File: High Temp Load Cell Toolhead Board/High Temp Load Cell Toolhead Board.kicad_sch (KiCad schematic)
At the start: 118 parts, among them J1 Conn_01x03, J11 Conn_01x03, J12 Conn_01x03, J13 PinHeader_2x4_P2.54mm, J2 Conn_02x08, J6 Conn_01x04, J7 Conn_01x02, J8 Conn_01x04, J9 Conn_01x02, P1 USB_C_Plug_USB2.0, Q1 DMG3404L, Q2 DMG3404L, SW1 SW_SPST, U1 MAX31865xTP, U2 STM32F103CBU6TR, U3 SN74LVC2G17DSFR, U4 SN74AHC1G32QDBVRQ1, U5 ADS1220, X1 ECS-2520MVLC-080-BP-TR

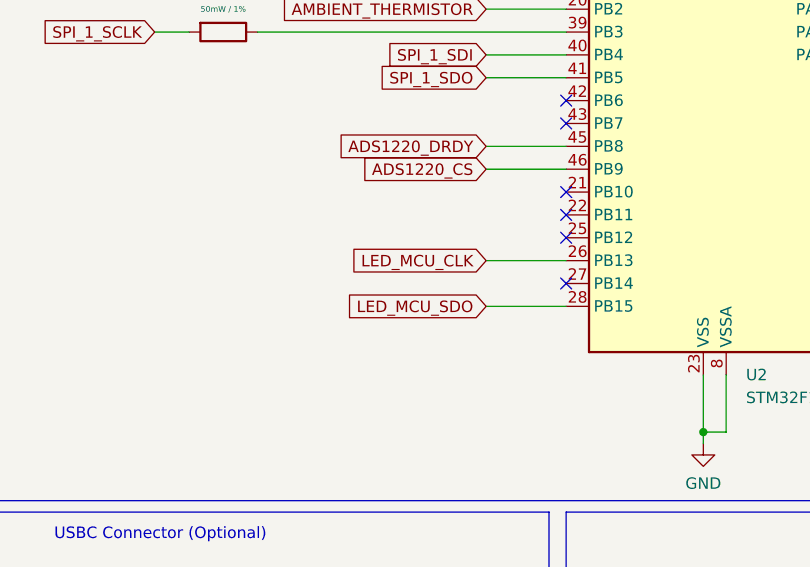
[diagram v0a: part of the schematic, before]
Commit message: USB Routing Improvement & Trach Width Change
* Fix net class assignment of USB lines so they autoroute with the correct rules.
* Moved the LED CLK line routing so it doesn't cross the USB lines
* Added a zone of ground fill on layer 3 to cover the USB traces on the back of the board
* Changes the standard track with to 15mil / 0.381mm. This is what OSH Park say is 50 Ohm in their process.

Fixup

Fixup
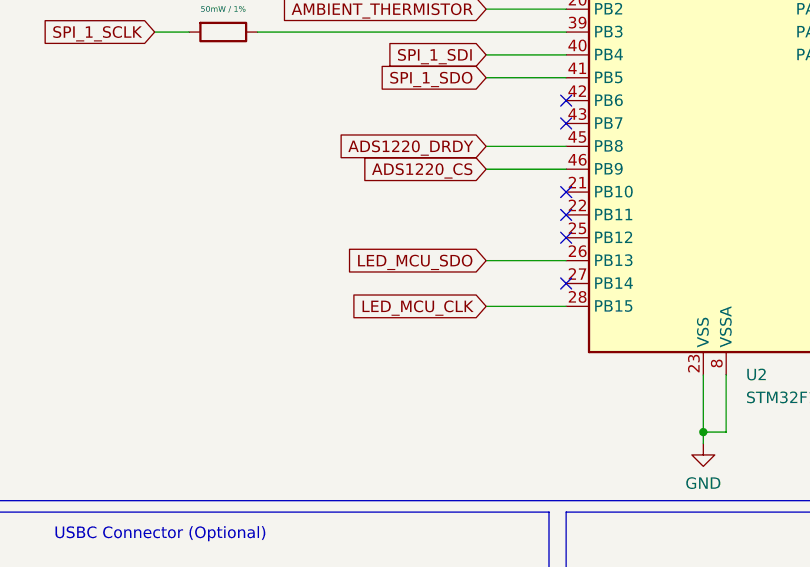
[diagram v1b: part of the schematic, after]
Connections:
- net LED_MCU_CLK: now also U2.28 (PB15); no longer U2.26 (PB13)
- net LED_MCU_SDO: now also U2.26 (PB13); no longer U2.28 (PB15)

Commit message: Replace Oscillator Module with Crystal
* After a bunch of research I've concluded that I cant use the Oscillator Module with Katapult's codebase for the STM32 chips. Added discussion on this to the design doc. Updated design to use a crystal and 2 caps. Exact capacitor values to be calculated later

* Based on the best advice I can find for decoupling capacitors on the MCU I have moved them to the back side of the board. This allows their footprints to overlap with the MCU itself, reducing the distance from the MCU to the decoupling cap. Also added vias next to the 2 pins  on the MCU that are true ground pins. There are other ground connections through GPIO pins but these are high impedance.

* Removed the power planes on layer 3 and replaced them with traces. With the additional components on the bottom layer, its more advantageous to have layer 3 be a ground reference for layer 4 in the places where items are routed on that layer. Power planes were easier to maintain but I don't think this board has any power delivery problems.

* Removed the extra diode and routing from the USB supply. Its not a requirement that the 5V rail power up from USB.
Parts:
- removed D16: 40V, 1A, SMA, Diode_SMD:D_SMA, symbol Device:D_Schottky
- removed X1: ECS-2520MVLC-080-BP-TR, Oscillator:Oscillator_SMD_ECS_2520MV-xxx-xx-4Pin_2.5x2.0mm, symbol Oscillator:ECS-2520MV-xxx-xx
- added C30, C33: 2?pF, Capacitor_SMD:C_0603_1608Metric, symbol Device:C
- added Y1: Crystal ECS-.327-6-34QCS-TR, ECS-.327-6-34QCS-TR:XTAL_ECS-.327-6-34QCS-TR, symbol Device:Crystal
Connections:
- net GND: now also U2.10 (PA0), U2.15 (PA5), U2.16 (PA6), U2.2 (PC13), U2.21 (PB10), U2.22 (PB11), U2.25 (PB12), U2.27 (PB14), U2.29 (PA8), U2.3 (PC14), U2.30 (PA9), U2.4 (PC15), U2.42 (PB6), U2.43 (PB7), C30.1, C33.1
- net OSC_IN: now reaches U2.5 (PD0)
- net OSC_IN: now also C30.2, Y1.2
- net OSC_OUT: now reaches U2.6 (PD1)
- net OSC_OUT: now also C33.2, Y1.1
- net SPI_1_SDO_OR_CS: now reaches AC1.13 (SDA/SDI/SDIO), U4.4
- net +5V_USB: now reaches D15.2 (A), P1.A4 (VBUS), P1.A9 (VBUS), P1.B4 (VBUS), P1.B9 (VBUS)
- no-connect marks 27 -> 11
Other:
- moved on the sheet: C20, C21, C22, C23, C24, C25, C26, D15, R13, R28, U2

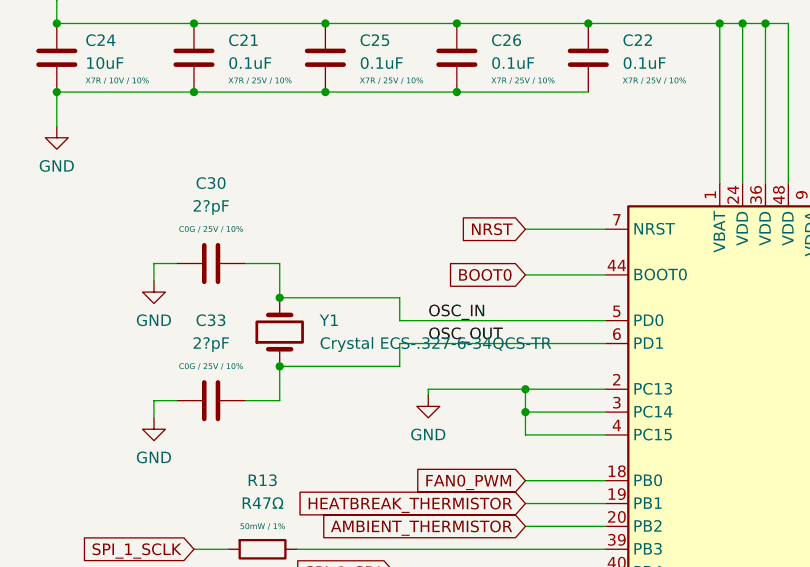
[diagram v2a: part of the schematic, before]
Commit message: Add Via Stitching
* Re-run via stitching on GND
* Add capacitor values to crystal caps
* Update design doc
* Remove bad assembly document
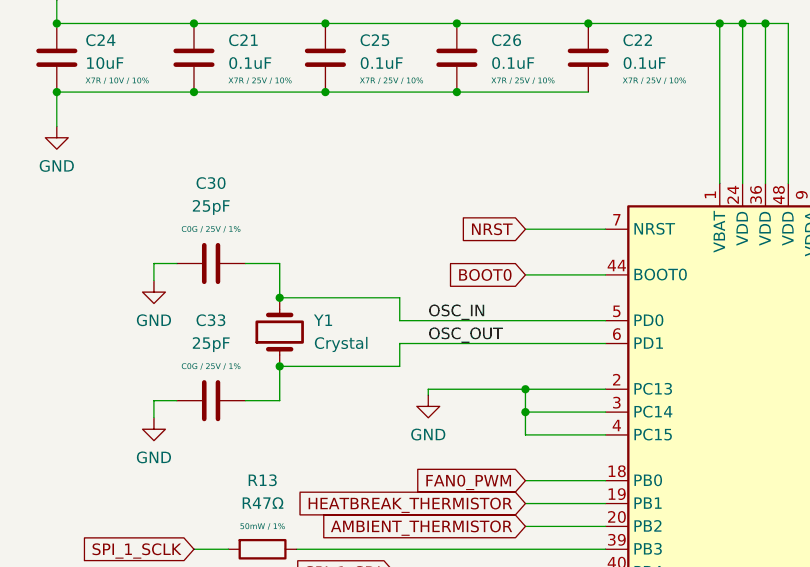
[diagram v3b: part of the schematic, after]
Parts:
- C30, C33: value 2?pF -> 25pF
- Y1: value Crystal ECS-.327-6-34QCS-TR -> Crystal
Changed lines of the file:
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@@
 			)
 		)
-		(property "Value" "2?pF"
+		(property "Value" "25pF"
 			(at 66.04 182.88 90)
 			(effects
@@
 			)
 		)
-		(property "Description" "C0G / 25V / 10%"
+		(property "Description" "C0G / 25V / 1%"
 			(at 66.04 185.42 90)
 			(effects
@@
 			)
 		)
-		(property "Value" "2?pF"
+		(property "Value" "25pF"
 			(at 66.04 198.12 90)
 			(effects
@@
 			)
 		)
-		(property "Description" "C0G / 25V / 10%"
+		(property "Description" "C0G / 25V / 1%"
 			(at 66.04 200.66 90)
 			(effects
@@
 		(fields_autoplaced yes)
 		(property "Reference" "Y1"
-			(at 78.105 195.5799 90)
+			(at 77.47 195.5799 90)
 			(effects
 				(font
@@
 			)
 		)
-		(property "Value" "Crystal ECS-.327-6-34QCS-TR"
-			(at 78.105 198.1199 90)
+		(property "Value" "Crystal"
+			(at 77.47 198.1199 90)
 			(effects
 				(font

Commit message: WIP Address community comments
* Switch to 6 layers and update design rules for new 6 layer process
* Change fan MOSFETs based on feedback. Drive MOSFETs with level shifter at 5V
* Add a 5V LDO for the loadcell thats not potentially poisoned by 5V LED noise
* Delete MAX chip, switch to PT1000
* Use 2 SPI busses, delete CS lines
* Move all components to front of board, re-organize layout to fit everything
* Switch to vertical USBC connector and import model

The schematic is updated but the routing has not been done
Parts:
- removed FID1, FID2, FID3: Fiducial, Fiducial:Fiducial_0.5mm_Mask1.5mm, symbol Mechanical:Fiducial
- removed R28: R430Ω, Resistor_SMD:R_0603_1608Metric, symbol Device:R
- removed U1: MAX31865xTP, Package_DFN_QFN:TQFN-20-1EP_5x5mm_P0.65mm_EP3.25x3.25mm, symbol Sensor_Temperature:MAX31865xTP
- removed U4: SN74AHC1G32QDBVRQ1, Package_TO_SOT_SMD:SOT-23-5, symbol 74xGxx:74AHC1G32
- added C37, C38: 0.1uF, Capacitor_SMD:C_0603_1608Metric, symbol Device:C
- added D16: RED LED, LED_SMD:LED_0603_1608Metric, symbol Device:LED
- added LDO3: TPS7A21-Q1 5V @ 500mA, Package_SON:VSON-8-1EP_3x3mm_P0.65mm_EP1.65x2.4mm_ThermalVias, symbol Project_Symbols:TPS7A21-Q1
- added R29: R1kΩ, Resistor_SMD:R_0603_1608Metric, symbol Device:R
- added R30, R32: R4.7kΩ, Resistor_SMD:R_0603_1608Metric, symbol Device:R
- added R31: R2.2kΩ, Resistor_SMD:R_0603_1608Metric, symbol Device:R
- added R33: R47Ω, Resistor_SMD:R_0603_1608Metric, symbol Device:R
- added TP1: Test +3V3, symbol Connector:TestPoint
- added TP2: Test +5V5, symbol Connector:TestPoint
- added TP3: Test +5V, symbol Connector:TestPoint
- added TP4: Test +5VA, symbol Connector:TestPoint
- added U1: SN74LVC2G17DSFR, Package_TO_SOT_SMD:SOT-363_SC-70-6, symbol SN74LVC2G17DSFR:SN74LVC2G17DSFR
- C10, C9: value 0.1uF -> 10uF; footprint Capacitor_SMD:C_0603_1608Metric -> Capacitor_SMD:C_1206_3216Metric
- LDO1: value TPS7121-Q1 5V @ 500mA -> TPS7A21-Q1 5V @ 500mA
- LDO2: value TPS7121-Q1 3.3V @ 500mA -> TPS7A21-Q1 3.3V @ 500mA
- P1: footprint Connector_USB:USB_C_Receptacle_GCT_USB4110 -> GCT_USB4145-03-0170-C:USB4145030170C; Manufacturer_Part_Number USB4110-GF-A -> USB4145-03-0170-C; Supplier_Link https://www.digikey.com/en/products/detail/gct/USB4110-GF-A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 -> https://www.digikey.com/en/products/detail/gct/USB4145-03-0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; Supplier_Part_Number 2073-USB4110-GF-A-1-ND -> 2073-USB4145-03-0170-CCT-ND
- Q1, Q2: value DMG3404L -> CSD17581Q3A; footprint Package_TO_SOT_SMD:SOT-23 -> Package_SON:VSON-8_3.3x3.3mm_P0.65mm_NexFET; symbol Transistor_FET:DMG3404L -> Transistor_FET:CSD17581Q3A; MANUFACTURER (none) -> Texas Instruments; MAXIMUM_PACKAGE_HEIGHT (none) -> 0.9mm; Manufacturer_Name Diodes Incorporated -> Texas Instruments; Manufacturer_Part_Number DMG3404L-7 -> CSD17581Q3A; PARTREV (none) -> October 2016; STANDARD (none) -> Manufacturer Recommendations; Supplier_Link https://www.digikey.com/en/products/detail/diodes-incorpora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 -> https://www.digikey.com/en/products/detail/texas-instrument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; Supplier_Part_Number DMG3404L-7DICT-ND -> 296-47754-1-ND
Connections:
- net ADS1220_CS is gone; now on net GND: U2.46 (PB9), U5.2 (~{CS})
- net ADXL345_CS is gone; now on net GND: AC1.7 (~{CS}), U2.11 (PA1)
- net +3V3: now also R30.2, R31.2, TP1.1; no longer C11.1, C9.1
- net +5V: now also TP3.1, U1.5 (VCC); no longer C13.2, C17.1, C29.1, L2.2, U5.12 (AVDD), U5.9 (REFP0)
- net +5V5: now also C9.1, LDO3.5 (EN), LDO3.8 (VIN), TP2.1
- net FAN0_MOSFET_GND: now also Q1.5 (D); no longer Q1.3 (D)
- net FAN0_PWM: now also U1.1 (1A); no longer R18.2, R19.2
- net FAN0_TACH: now also C37.1
- net FAN1_MOSFET_GND: now also Q2.5 (D); no longer Q2.3 (D)
- net FAN1_PWM: now also U1.3 (2A); no longer R26.2, R8.2
- net FAN1_TACH: now also C11.1
- net GND: now also C10.2, L13.2, Q1.1 (S), Q1.3 (S), Q2.1 (S), Q2.3 (S), C37.2, C38.2, D16.1 (K), LDO3.2 (GND), LDO3.3 (GND), LDO3.4 (GND), LDO3.6 (GND), LDO3.7 (GND), LDO3.9 (GND), U1.2 (GND); no longer U2.27 (PB14), U2.29 (PA8), U2.42 (PB6), U2.43 (PB7)
- net LED_GND: now also J8.1 (Pin_1); no longer J8.4 (Pin_4)
- net LED_MCU_CLK: now also U2.43 (PB7); no longer U2.28 (PB15)
- net LED_MCU_SDO: now also U2.42 (PB6); no longer U2.26 (PB13)
- net LED_POWER: now also J8.4 (Pin_4); no longer J8.1 (Pin_1)
- net SPI_1_SCLK: no longer AC1.14 (SCL/SCLK)
- net SPI_1_SDI: no longer AC1.12 (SDO/ALT_ADDRESS)
- net at R19.1: now also Q1.4 (G); no longer Q1.1 (G)
- net at L12.1: now also R30.1, R31.1, R32.2; no longer C10.1
- net at R26.1: now also Q2.4 (G); no longer Q2.1 (G)
- net MAX31865_CS renamed PT1000
- net PT1000: now also C38.1, R32.1
- net PT100+ renamed PT1000+
- net PT100- renamed PT1000-
- net SPI_1_SDO_OR_CS renamed SPI_2_SDO
- net SPI_2_SDO: now also U2.28 (PB15)
- new net: R33.1, U2.26 (PB13)
- new net: D16.2 (A), R29.1
- new net +5VA: C10.1, C13.2, C17.1, C29.1, L2.2, LDO3.1 (VOUT), TP4.1, U5.12 (AVDD), U5.9 (REFP0)
- new net FAN0_PWM_+5V: R18.2, R19.2, U1.6 (1Y)
- new net FAN1_PWM_+5V: R26.2, R8.2, U1.4 (2Y)
- new net INDICATOR_LED: R29.2, U2.29 (PA8)
- new net SPI_2_SCLK: AC1.14 (SCL/SCLK), R33.2
- new net SPI_2_SDI: AC1.12 (SDO/ALT_ADDRESS), U2.27 (PB14)
- no-connect marks 11 -> 10
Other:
- note added: "3.3V to 5V Fan PWM Level Shifter"
- note added: "5.5V to 3.3V LDO"
- note added: "5.5V to 5V LED Power LDO"
- note added: "5.5V to 5V Load Cell Power LDO"
- note added: "PT1000 Port"
- note added: "Test Points"
- note removed: "6V to 3.3V LDO"
- note removed: "6V to 5V LDO"
- note removed: "MAX31865 RTD Sensor"
- moved on the sheet: C1, C12, C13, C14, C15, C16, C17, C2, C20, C21, C22, C23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

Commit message: Feedback Updates Completed
* Disconnected unused GPIO pins from ground, use software pulldown instead.
* Re-rout for OSHPark's 6 layer stackup
* Shrink reference text to 0.8mmx0.8mm and 5 mil thickness
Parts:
- removed R31: R2.2kΩ, Resistor_SMD:R_0603_1608Metric, symbol Device:R
- removed R32: R4.7kΩ, Resistor_SMD:R_0603_1608Metric, symbol Device:R
- removed TP1: Test +3V3, symbol Connector:TestPoint
- removed TP2: Test +5V5, symbol Connector:TestPoint
- removed TP3: Test +5V, symbol Connector:TestPoint
- removed TP4: Test +5VA, symbol Connector:TestPoint
- added D17: RED LED, LED_SMD:LED_0603_1608Metric, symbol Device:LED
- added R12: R2kΩ, Resistor_SMD:R_0603_1608Metric, symbol Device:R
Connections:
- net PT1000 is gone; now on net HOTEND_THERMISTOR: C38.1, U2.12 (PA2)
- net +5VA: now also R12.2
- net FAN0_TACH: now also U2.14 (PA4); no longer U2.17 (PA7)
- net FAN1_PWM: now also U2.15 (PA5); no longer U2.14 (PA4)
- net GND: now also D17.1 (K); no longer U2.10 (PA0), U2.11 (PA1), U2.15 (PA5), U2.16 (PA6), U2.2 (PC13), U2.21 (PB10), U2.22 (PB11), U2.25 (PB12), U2.3 (PC14), U2.30 (PA9), U2.4 (PC15), U2.46 (PB9)
- net HOTEND_THERMISTOR: now reaches L12.1, R30.1
- net AIN0: now reaches C14.1, C15.2, R17.1, U5.11 (AIN0/REFP1)
- net AIN1: now reaches C14.2, C16.1, R16.1, U5.10 (AIN1)
- net PT1000+ renamed HOTEND_TH_GND
- net HOTEND_TH_GND: now also L13.1; no longer L12.2
- net PT1000- renamed HOTEND_TH_VREF
- net HOTEND_TH_VREF: now also L12.2; no longer L13.1
- new net: D17.2 (A), R12.1
- no-connect marks 10 -> 22
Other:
- note added: "Hotend Thermistor"
- note removed: "PT1000 Port"
- note removed: "Test Points"
- moved on the sheet: AC1, C11, C12, C13, C14, C15, C16, C17, C19, C27, C28, C29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

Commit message: Update 5V Power input
* Changed 5V USB power to rout in via the main 24V power input. This assumes the buck converter can operate in dropout mode and pass the 5V supply to the LDOs. This avoids potential issues with backfeeding the buck converter.
* Added a klipper pins file to give meaningful names to pins
* Added do-not-populate bypass resistors for fans to test tachometer behavior
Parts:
- added R20, R24: R20kΩ, Resistor_SMD:R_0603_1608Metric, symbol Device:R
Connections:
- net +24V: now also D15.1 (K)
- net +5V5: no longer D15.1 (K)
- net FAN0_MOSFET_GND: now also R20.2
- net FAN1_MOSFET_GND: now also R24.2
- net GND: now also R20.1, R24.1
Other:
- moved on the sheet: C11, C37, D7, D8, Q1, Q2, R14, R18, R19, R26, R4, R8

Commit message: Add Dotstar Indicator
This change replaces the indicator LED with a Dotstar RGB LED. This allows various conditions to be indicated at the toolhead via colors, brightness and blinking.

* Fixed missing guard ring on layers 4 and 5.
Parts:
- removed D16: RED LED, LED_SMD:LED_0603_1608Metric, symbol Device:LED
- removed R29: R1kΩ, Resistor_SMD:R_0603_1608Metric, symbol Device:R
- added D16: DotStar Micro LED, LED_SMD:LED-APA102-2020, symbol LED:APA102-2020
- added U4: SN74LVC2G17DSFR, Package_TO_SOT_SMD:SOT-363_SC-70-6, symbol SN74LVC2G17DSFR:SN74LVC2G17DSFR
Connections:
- net +5V: now also D16.1 (VDD), U4.5 (VCC)
- net GND: now also D16.6 (GND), U4.2 (GND)
- net INDICATOR_LED_SDO: now reaches U2.30 (PA9)
- net INDICATOR_LED_SDO: now also U4.3 (2A)
- net INDICATOR_LED renamed INDICATOR_LED_CLK
- net INDICATOR_LED_CLK: now also U4.1 (1A)
- new net RGB_INDICATOR_CLK: D16.5 (CKI), U4.4 (2Y)
- new net RGB_INDICATOR_SDO: D16.4 (SDI), U4.6 (1Y)
- no-connect marks 22 -> 23
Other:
- note added: "RGB INDICATOR LED"
- moved on the sheet: D13, D14, D17, D2, D3, D5, D6, H1, H2, H3, H4, R10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

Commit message: Move Filament Switch & Heatbreak Thermistor to ADC Inputs
* Move Filament switch line from PA15 to PA7
* Move Heatberak Thermistor from PB1 to PA6 (PB1 is Boot1)
* Re-routed Filament switch line on the back side of the PCB
* Edited pin assignments for thermistors to make routing cleaner
* Updated pins file to reflect changes
* Renamed Neopixel port to Dotstar.
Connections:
- net AMBIENT_THERMISTOR: now also U2.19 (PB1); no longer U2.20 (PB2)
- net FILAMENT_SW: now also U2.17 (PA7); no longer U2.38 (PA15)
- net HEATBREAK_THERMISTOR: now also U2.16 (PA6); no longer U2.19 (PB1)
- net INDICATOR_LED_CLK renamed RGB_LED_CLOCK
- net INDICATOR_LED_SDO renamed RGB_LED_DATA
- net LED_MCU_CLK renamed DOTSTAR_LED_CLOCK
- net LED_MCU_SDO renamed DOTSTAR_LED_DATA
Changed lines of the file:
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@@
 	)
 	(no_connect
+		(at 138.43 221.615)
+	)
+	(no_connect
+		(at 105.41 216.535)
+	)
+	(no_connect
 		(at 67.945 317.5)
 	)
@@
 	)
 	(no_connect
-		(at 138.43 201.295)
-	)
-	(no_connect
 		(at 105.41 239.395)
 	)
@@
 	)
 	(no_connect
-		(at 138.43 198.755)
-	)
-	(no_connect
 		(at 560.705 191.77)
 	)
@@
 	(wire
 		(pts
+			(xy 140.335 198.755) (xy 138.43 198.755)
+		)
+		(stroke
+			(width 0)
+			(type default)
+		)
+	)
+	(wire
+		(pts
 			(xy 103.505 224.155) (xy 105.41 224.155)
 		)
@@
 	(wire
 		(pts
-			(xy 105.41 216.535) (xy 103.505 216.535)
-		)
-		(stroke
-			(width 0)
-			(type default)
-		)
-	)
-	(wire
-		(pts
 			(xy 441.325 379.73) (xy 441.325 374.015)
 		)
@@
 	(wire
 		(pts
+			(xy 140.335 201.295) (xy 138.43 201.295)
+		)
+		(stroke
+			(width 0)
+			(type default)
+		)
+	)
+	(wire
+		(pts
 			(xy 76.2 353.06) (xy 95.25 353.06)
 		)
@@
 	(wire
 		(pts
-			(xy 140.335 221.615) (xy 138.43 221.615)
-		)
-		(stroke
-			(width 0)
-			(type default)
-		)
-	)
-	(wire
-		(pts
 			(xy 52.705 180.34) (xy 52.705 195.58)
 		)
@@
 				)
 				(justify right)
+				(hide yes)
 			)
 		)
@@
 				)
 				(justify left)
+				(hide yes)
 			)
 		)
@@
 				)
 				(justify right)
+				(hide yes)
 			)
 		)
@@
 				)
 				(justify left)
+				(hide yes)
 			)
 		)
@@
 		)
 	)
+	(global_label "HEATBREAK_THERMISTOR"
+		(shape input)
+		(at 140.335 198.755 0)
+		(fields_autoplaced yes)
+		(effects
+			(font
+				(size 1.27 1.27)
+			)
+			(justify left)
+		)
+		(property "Intersheetrefs" "${INTERSHEET_REFS}"
+			(at 166.422 198.755 0)
+			(effects
+				(font
+					(size 1.27 1.27)
+				)
+				(justify left)
+				(hide yes)
+			)
+		)
+	)
 	(global_label "USB_PULL_UP"
 		(shape input)
@@
 		)
 	)
-	(global_label "HEATBREAK_THERMISTOR"
+	(global_label "FAN1_TACH"
 		(shape input)
-		(at 103.505 213.995 180)
+		(at 433.705 361.315 180)
 		(fields_autoplaced yes)
 		(effects
@@
 		)
 		(property "Intersheetrefs" "${INTERSHEET_REFS}"
-			(at 77.418 213.995 0)
+			(at 420.3783 361.315 0)
 			(effects
 				(font
@@
 		)
 	)
-	(global_label "FAN1_TACH"
+	(global_label "FILAMENT_SW"
 		(shape input)
-		(at 433.705 361.315 180)
+		(at 140.335 201.295 0)
 		(fields_autoplaced yes)
 		(effects
@@
 				(size 1.27 1.27)
 			)
-			(justify right)
+			(justify left)
 		)
 		(property "Intersheetrefs" "${INTERSHEET_REFS}"
-			(at 420.3783 361.315 0)
+			(at 155.6573 201.295 0)
 			(effects
 				(font
 					(size 1.27 1.27)
 				)
-				(justify right)
+				(justify left)
 				(hide yes)
 			)
 		)
 	)
-	(global_label "LED_MCU_SDO"
+	(global_label "DOTSTAR_LED_DATA"
 		(shape input)
 		(at 103.505 226.695 180)
@@
 		)
 	)
-	(global_label "AMBIENT_THERMISTOR"
-		(shape input)
-		(at 103.505 216.535 180)
-		(fields_autoplaced yes)
-		(effects
-			(font
-				(size 1.27 1.27)
-			)
-			(justify right)
-		)
-		(property "Intersheetrefs" "${INTERSHEET_REFS}"
-			(at 80.1394 216.535 0)
-			(effects
-				(font
-					(size 1.27 1.27)
-				)
-				(justify right)
-				(hide yes)
-			)
-		)
-	)
 	(global_label "FAN0_PWM"
 		(shape input)
@@
 		)
 	)
-	(global_label "INDICATOR_LED_CLK"
+	(global_label "RGB_LED_CLOCK"
 		(shape input)
 		(at 140.335 203.835 0)
@@
 		)
 	)
-	(global_label "FILAMENT_SW"
-		(shape input)
-		(at 140.335 221.615 0)
-		(fields_autoplaced yes)
-		(effects
-			(font
-				(size 1.27 1.27)
-			)
-			(justify left)
-		)
-		(property "Intersheetrefs" "${INTERSHEET_REFS}"
-			(at 155.6573 221.615 0)
-			(effects
-				(font
-					(size 1.27 1.27)
-				)
-				(justify left)
-				(hide yes)
-			)
-		)
-	)
 	(global_label "SW_CLK"
 		(shape input)
@@
 		)
 	)
-	(global_label "LED_MCU_CLK"
+	(global_label "DOTSTAR_LED_CLOCK"
 		(shape input)
 		(at 103.505 229.235 180)
@@
 		)
 	)
-	(global_label "INDICATOR_LED_SDO"
+	(global_label "RGB_LED_DATA"
 		(shape input)
 		(at 140.335 206.375 0)
@@
 		)
 	)
+	(global_label "AMBIENT_THERMISTOR"
+		(shape input)
+		(at 103.505 213.995 180)
+		(fields_autoplaced yes)
+		(effects
+			(font
+				(size 1.27 1.27)
+			)
+			(justify right)
+		)
+		(property "Intersheetrefs" "${INTERSHEET_REFS}"
+			(at 80.1394 213.995 0)
+			(effects
+				(font
+					(size 1.27 1.27)
+				)
+				(justify right)
+				(hide yes)
+			)
+		)
+	)
 	(global_label "SW_CLK"
 		(shape input)
@@
 		)
 	)
-	(global_label "INDICATOR_LED_CLK"
+	(global_label "RGB_LED_CLOCK"
 		(shape input)
 		(at 480.06 191.135 180)
@@
 		)
 	)
-	(global_label "LED_MCU_SDO"
+	(global_label "DOTSTAR_LED_DATA"
 		(shape input)
 		(at 288.29 52.705 180)
@@
 		)
 	)
-	(global_label "INDICATOR_LED_SDO"
+	(global_label "RGB_LED_DATA"
 		(shape input)
 		(at 480.06 196.215 180)
@@
 		)
 	)
-	(global_label "LED_MCU_CLK"
+	(global_label "DOTSTAR_LED_CLOCK"
 		(shape input)
 		(at 288.29 57.785 180)
